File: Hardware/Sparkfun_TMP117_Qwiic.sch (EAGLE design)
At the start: 22 parts, among them J1 PTH, U2 TMP117

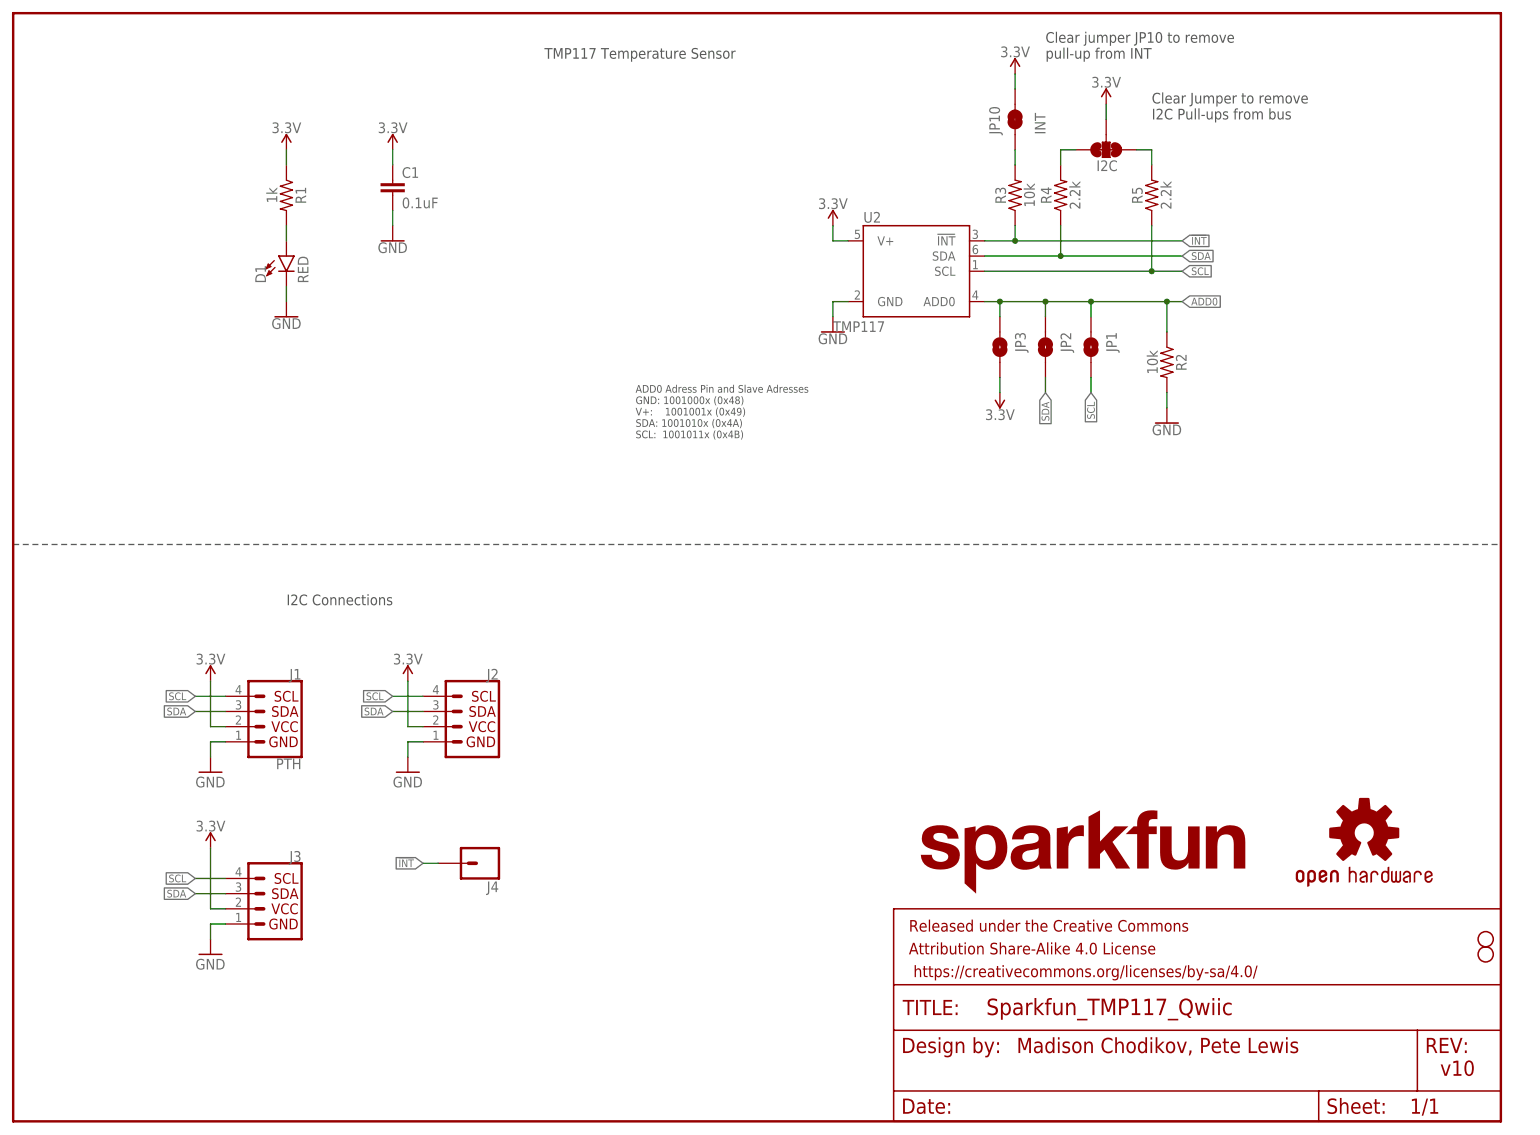
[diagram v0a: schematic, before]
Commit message: more layout changes
-moved to 4 jumpers on address select, to fully remove pull resisor when you cut trace. Previous version had pull down resistor permenantly in circuit, so it would be tied to SDA or SCL when those address options were selected.
-SCH cleanup
-rerouting as necessary.
-added LED bypass jumper
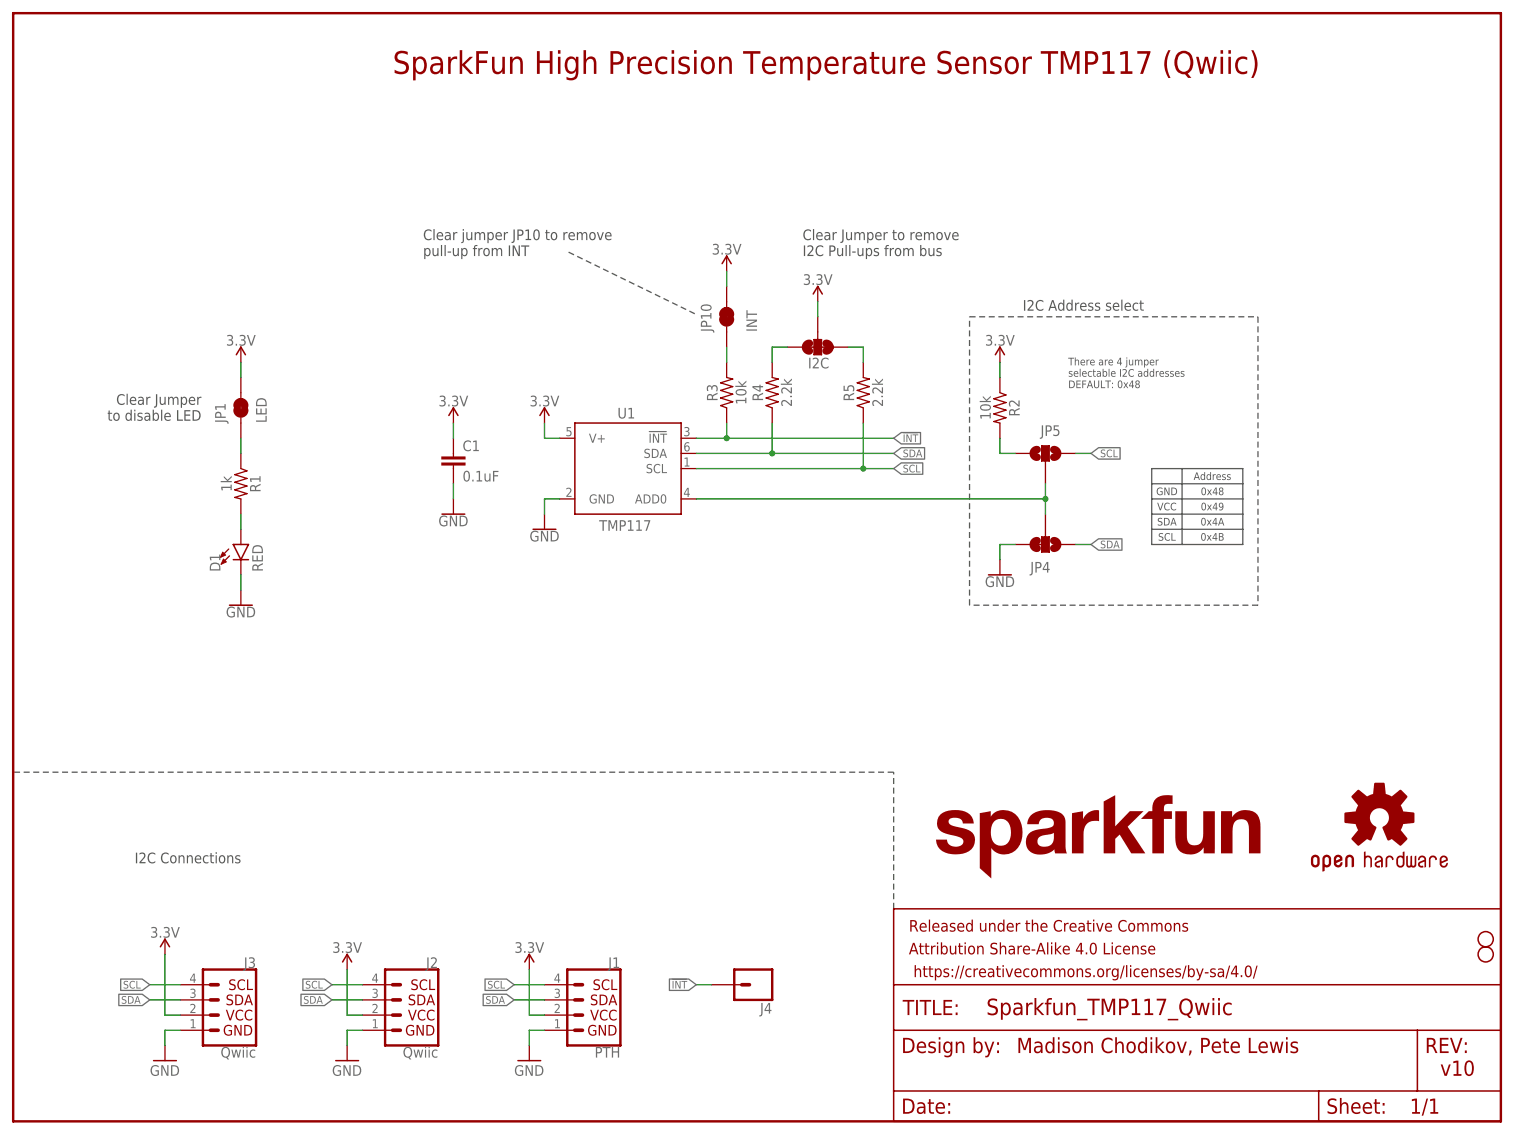
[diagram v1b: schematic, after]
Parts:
- removed JP2, JP3: JUMPER-SMT_2_NO_SILK, SparkFun-Jumpers:JUMPER-SMT_2_NO_SILK
- removed U2: TMP117, TMP117:TMP117
- added JP4: JUMPER-SMT_3_1-NC_TRACE_NO-SILK, SparkFun-Jumpers:JUMPER-SMT_3_1-NC_TRACE_NO-SILK
- added JP5: JUMPER-SMT_3_NO_NO_SILK, SparkFun-Jumpers:JUMPER-SMT_3_NO_NO_SILK
- added U1: TMP117, TMP117:TMP117
- J2, J3: value (none) -> Qwiic
- JP1: value JUMPER-SMT_2_NO_SILK -> LED; device SparkFun-Jumpers:JUMPER-SMT_2_NO_SILK -> SparkFun-Jumpers:JUMPER-SMT_2_NC_TRACE_SILK
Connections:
- new net N$7: JP5.1, R2.2
- new net N$8: JP1.1, R1.1
- net !INT: now also U1.!INT; no longer U2.!INT
- net 3.3V: now also JP1.2, R2.1, U1.V+; no longer JP3.2, R1.1, U2.V+
- net ADD0: now also JP4.2, JP5.2, U1.ADD0; no longer JP1.1, JP2.1, JP3.1, R2.1, U2.ADD0
- net GND: now also JP4.3, U1.GND; no longer R2.2, U2.GND
- net SCL: now also JP5.3, U1.SCL; no longer JP1.2, U2.SCL
- net SDA: now also JP4.1, U1.SDA; no longer JP2.2, U2.SDA
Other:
- note added: "0x48"
- note added: "0x49"
- note added: "0x4A"
- note added: "0x4B"
- note added: "Address"
- note added: "Clear Jumper to disable LED"
- note added: "GND"
- note added: "I2C Address select"
- note added: "SCL"
- note added: "SDA"
- note added: "SparkFun High Precision Temperature Sensor TMP117 (Qwiic)"
- note added: "There are 4 jumper selectable I2C addresses DEFAULT: 0x48"
- note added: "VCC"
- note removed: "ADD0 Adress Pin and Slave Adresses GND: 1001000x (0x48) V+: 1001001x (0x49) SDA: 1001010x (0x4A) SCL: 1001011x (0x4B)"
- note removed: "TMP117 Temperature Sensor"
- moved on the sheet: C1, D1, I2C, J1, J2, J3, J4, JP10, R1, R2, R3, R4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

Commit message: post design review changes
-Added fiducials
-added bottom two standoffs
-switched to SFE logo with flame
-moved I2C jumper to bottom
-added outer box silk to address jumpers
-moved pwr LED and jumper to make room for standoff
-changes all traces to 8 mil, except 3.3V power up to 16 mil.
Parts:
- removed LOGO2: SFE_LOGO_NAME.1_INCH, SparkFun-Aesthetics:SFE_LOGO_NAME.1_INCH
- added FD1, FD2, FD3, FD4: FIDUCIALUFIDUCIAL, SparkFun-Aesthetics:FIDUCIALUFIDUCIAL
- added JP2, JP3: STAND-OFF, SparkFun:STAND-OFF
- added LOGO4: SFE_LOGO_NAME_FLAME.1_INCH, SparkFun-Aesthetics:SFE_LOGO_NAME_FLAME.1_INCH
- JP10: device SparkFun-Passives:JUMPER-PAD-2-NC_BY_TRACE -> SparkFun-Jumpers:JUMPER-SMT_2_NC_TRACE_SILK
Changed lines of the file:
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@@
 <part name="JP9" library="SparkFun" deviceset="STAND-OFF" device=""/>
 <part name="I2C" library="SparkFun-Jumpers" library_urn="urn:adsk.eagle:library:528" deviceset="JUMPER-SMT_3_2-NC_TRACE" device="_SILK" package3d_urn="urn:adsk.eagle:package:39289/1" value=""/>
-<part name="JP10" library="SparkFun-Passives" deviceset="JUMPER-PAD-2-NC_BY_TRACE" device="" value="INT"/>
+<part name="JP10" library="SparkFun-Jumpers" deviceset="JUMPER-SMT_2_NC_TRACE" device="_SILK" value="INT"/>
 <part name="U1" library="TMP117" deviceset="TMP117" device=""/>
-<part name="LOGO2" library="SparkFun-Aesthetics" deviceset="SFE_LOGO_NAME" device=".1_INCH"/>
 <part name="JP4" library="SparkFun-Jumpers" deviceset="JUMPER-SMT_3_1-NC_TRACE" device="_NO-SILK"/>
 <part name="GND8" library="SparkFun-PowerSymbols" deviceset="GND" device=""/>
@@
 <part name="SUPPLY10" library="SparkFun-PowerSymbols" library_urn="urn:adsk.eagle:library:530" deviceset="3.3V" device=""/>
 <part name="JP1" library="SparkFun-Jumpers" library_urn="urn:adsk.eagle:library:528" deviceset="JUMPER-SMT_2_NC_TRACE" device="_SILK" package3d_urn="urn:adsk.eagle:package:39281/1" value="LED"/>
+<part name="JP2" library="SparkFun" deviceset="STAND-OFF" device=""/>
+<part name="JP3" library="SparkFun" deviceset="STAND-OFF" device=""/>
+<part name="LOGO4" library="SparkFun-Aesthetics" deviceset="SFE_LOGO_NAME_FLAME" device=".1_INCH"/>
+<part name="FD1" library="SparkFun-Aesthetics" library_urn="urn:adsk.eagle:library:507" deviceset="FIDUCIAL" device="UFIDUCIAL" package3d_urn="urn:adsk.eagle:package:37111/1"/>
+<part name="FD2" library="SparkFun-Aesthetics" library_urn="urn:adsk.eagle:library:507" deviceset="FIDUCIAL" device="UFIDUCIAL" package3d_urn="urn:adsk.eagle:package:37111/1"/>
+<part name="FD3" library="SparkFun-Aesthetics" library_urn="urn:adsk.eagle:library:507" deviceset="FIDUCIAL" device="UFIDUCIAL" package3d_urn="urn:adsk.eagle:package:37111/1"/>
+<part name="FD4" library="SparkFun-Aesthetics" library_urn="urn:adsk.eagle:library:507" deviceset="FIDUCIAL" device="UFIDUCIAL" package3d_urn="urn:adsk.eagle:package:37111/1"/>
 </parts>
 <sheets>
@@
 <attribute name="VALUE" x="98.044" y="98.806" size="1.778" layer="96"/>
 </instance>
-<instance part="LOGO2" gate="G$1" x="152.4" y="40.64" smashed="yes"/>
 <instance part="JP4" gate="G$1" x="172.72" y="96.52" smashed="yes" rot="R270">
 <attribute name="NAME" x="170.18" y="91.821" size="1.778" layer="95" font="vector"/>
@@
 <attribute name="VALUE" x="40.64" y="116.84" size="1.778" layer="96" font="vector" rot="R90" align="top-left"/>
 </instance>
+<instance part="JP2" gate="G$1" x="243.84" y="30.48" smashed="yes"/>
+<instance part="JP3" gate="G$1" x="243.84" y="27.94" smashed="yes"/>
+<instance part="LOGO4" gate="G$1" x="152.4" y="38.1" smashed="yes"/>
+<instance part="FD1" gate="G$1" x="238.76" y="30.48" smashed="yes"/>
+<instance part="FD2" gate="G$1" x="241.3" y="30.48" smashed="yes"/>
+<instance part="FD3" gate="G$1" x="238.76" y="27.94" smashed="yes"/>
+<instance part="FD4" gate="G$1" x="241.3" y="27.94" smashed="yes"/>
 </instances>
 <busses>

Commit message: parts to SFE libraries
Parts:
- J1: device SparkX:I2C_STANDARD_NO_SILK -> SparkFun-Connectors:I2C_STANDARD_NO_SILK
- J2, J3: value Qwiic -> QWIIC_RA
- U1: device TMP117:TMP117 -> SparkFun-Sensors:TMP117
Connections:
- net 3.3V: now also J1.2; no longer J1.VCC
- net GND: now also J1.1; no longer J1.GND
- net SCL: now also J1.4; no longer J1.SCL
- net SDA: now also J1.3; no longer J1.SDA
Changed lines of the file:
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@@
 <part name="C1" library="SparkFun-Capacitors" deviceset="0.1UF" device="-0603-25V-(+80/-20%)" value="0.1uF"/>
 <part name="GND4" library="SparkFun-PowerSymbols" deviceset="GND" device=""/>
-<part name="J1" library="SparkX" deviceset="I2C_STANDARD" device="_NO_SILK" value="PTH"/>
-<part name="J3" library="SparkFun-Connectors" deviceset="QWIIC_CONNECTOR" device="JS-1MM" value="Qwiic"/>
+<part name="J1" library="SparkFun-Connectors" deviceset="I2C_STANDARD" device="_NO_SILK" value="PTH"/>
+<part name="J3" library="SparkFun-Connectors" deviceset="QWIIC_CONNECTOR" device="JS-1MM" value="QWIIC_RA"/>
 <part name="J4" library="SparkFun-Connectors" deviceset="CONN_01" device="PTH_NO_SILK_YES_STOP"/>
 <part name="LOGO1" library="SparkFun-Aesthetics" deviceset="OSHW-LOGO" device="MINI"/>
@@
 <part name="SUPPLY8" library="SparkFun-PowerSymbols" library_urn="urn:adsk.eagle:library:530" deviceset="3.3V" device=""/>
 <part name="SUPPLY9" library="SparkFun-PowerSymbols" library_urn="urn:adsk.eagle:library:530" deviceset="3.3V" device=""/>
-<part name="J2" library="SparkFun-Connectors" deviceset="QWIIC_CONNECTOR" device="JS-1MM" value="Qwiic"/>
+<part name="J2" library="SparkFun-Connectors" deviceset="QWIIC_CONNECTOR" device="JS-1MM" value="QWIIC_RA"/>
 <part name="JP8" library="SparkFun" deviceset="STAND-OFF" device=""/>
 <part name="JP9" library="SparkFun" deviceset="STAND-OFF" device=""/>
 <part name="I2C" library="SparkFun-Jumpers" library_urn="urn:adsk.eagle:library:528" deviceset="JUMPER-SMT_3_2-NC_TRACE" device="_SILK" package3d_urn="urn:adsk.eagle:package:39289/1" value=""/>
 <part name="JP10" library="SparkFun-Jumpers" deviceset="JUMPER-SMT_2_NC_TRACE" device="_SILK" value="INT"/>
-<part name="U1" library="TMP117" deviceset="TMP117" device=""/>
+<part name="U1" library="SparkFun-Sensors" deviceset="TMP117" device=""/>
 <part name="JP4" library="SparkFun-Jumpers" deviceset="JUMPER-SMT_3_1-NC_TRACE" device="_NO-SILK"/>
 <part name="GND8" library="SparkFun-PowerSymbols" deviceset="GND" device=""/>
@@
 <pinref part="GND5" gate="1" pin="GND"/>
 <wire x1="86.36" y1="12.7" x2="86.36" y2="15.24" width="0.1524" layer="91"/>
-<pinref part="J1" gate="G$1" pin="GND"/>
+<pinref part="J1" gate="G$1" pin="1"/>
 <wire x1="86.36" y1="15.24" x2="88.9" y2="15.24" width="0.1524" layer="91"/>
 </segment>
@@
 <pinref part="SUPPLY3" gate="G$1" pin="3.3V"/>
 <wire x1="86.36" y1="25.4" x2="86.36" y2="17.78" width="0.1524" layer="91"/>
-<pinref part="J1" gate="G$1" pin="VCC"/>
+<pinref part="J1" gate="G$1" pin="2"/>
 <wire x1="86.36" y1="17.78" x2="88.9" y2="17.78" width="0.1524" layer="91"/>
 </segment>
@@
 <net name="SDA" class="0">
 <segment>
-<pinref part="J1" gate="G$1" pin="SDA"/>
+<pinref part="J1" gate="G$1" pin="3"/>
 <wire x1="83.82" y1="20.32" x2="88.9" y2="20.32" width="0.1524" layer="91"/>
 <label x="83.82" y="20.32" size="1.27" layer="95" rot="R180" xref="yes"/>
@@
 </segment>
 <segment>
-<pinref part="J1" gate="G$1" pin="SCL"/>
+<pinref part="J1" gate="G$1" pin="4"/>
 <wire x1="88.9" y1="22.86" x2="83.82" y2="22.86" width="0.1524" layer="91"/>
 <label x="83.82" y="22.86" size="1.27" layer="95" rot="R180" xref="yes"/>

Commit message: 1st run of checklist
-version font type in schematic
-silk width bumped up to 8 mils on a couple jumpers and the tmp117 package
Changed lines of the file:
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@@
 <part name="JP8" library="SparkFun" deviceset="STAND-OFF" device=""/>
 <part name="JP9" library="SparkFun" deviceset="STAND-OFF" device=""/>
-<part name="I2C" library="SparkFun-Jumpers" library_urn="urn:adsk.eagle:library:528" deviceset="JUMPER-SMT_3_2-NC_TRACE" device="_SILK" package3d_urn="urn:adsk.eagle:package:39289/1" value=""/>
-<part name="JP10" library="SparkFun-Jumpers" deviceset="JUMPER-SMT_2_NC_TRACE" device="_SILK" value="INT"/>
+<part name="I2C" library="SparkFun-Jumpers" deviceset="JUMPER-SMT_3_2-NC_TRACE" device="_SILK" package3d_urn="urn:adsk.eagle:package:39289/1" value="JUMPER-SMT_3_2-NC_TRACE_SILK"/>
+<part name="JP10" library="SparkFun-Jumpers" deviceset="JUMPER-SMT_2_NC_TRACE" device="_SILK" package3d_urn="urn:adsk.eagle:package:39281/1" value="INT"/>
 <part name="U1" library="SparkFun-Sensors" deviceset="TMP117" device=""/>
 <part name="JP4" library="SparkFun-Jumpers" deviceset="JUMPER-SMT_3_1-NC_TRACE" device="_NO-SILK"/>
@@
 <part name="JP5" library="SparkFun-Jumpers" deviceset="JUMPER-SMT_3_NO" device="_NO_SILK" value="JUMPER-SMT_3_NO_NO_SILK"/>
 <part name="SUPPLY10" library="SparkFun-PowerSymbols" library_urn="urn:adsk.eagle:library:530" deviceset="3.3V" device=""/>
-<part name="JP1" library="SparkFun-Jumpers" library_urn="urn:adsk.eagle:library:528" deviceset="JUMPER-SMT_2_NC_TRACE" device="_SILK" package3d_urn="urn:adsk.eagle:package:39281/1" value="LED"/>
+<part name="JP1" library="SparkFun-Jumpers" deviceset="JUMPER-SMT_2_NC_TRACE" device="_SILK" package3d_urn="urn:adsk.eagle:package:39281/1" value="LED"/>
 <part name="JP2" library="SparkFun" deviceset="STAND-OFF" device=""/>
 <part name="JP3" library="SparkFun" deviceset="STAND-OFF" device=""/>
@@
 <text x="68.58" y="144.78" size="1.778" layer="97" font="vector">Clear jumper JP10 to remove
 pull-up from INT</text>
-<text x="238.76" y="7.62" size="2.54" layer="94">v10</text>
+<text x="238.76" y="7.62" size="2.54" layer="94" font="vector">v10</text>
 <text x="176.53" y="122.682" size="1.27" layer="97" font="vector">There are 4 jumper
 selectable I2C addresses

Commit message: checklist catches
-remove package value on jumpers (SCH)
-added VCC range text obj
-fixed drc errors cause by unconnected dimension wires on special route out stuff near IC
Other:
- note added: "(When using other qwiic ecosystem boards, only use 3.3V)"
- note added: "Madison Chodikov"
- note added: "Revised by: Pete Lewis"
- note added: "VCC RANGE: 1.8V to 5.5V"
- note removed: "Madison Chodikov, Pete Lewis"
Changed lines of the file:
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@@
 <part name="JP8" library="SparkFun" deviceset="STAND-OFF" device=""/>
 <part name="JP9" library="SparkFun" deviceset="STAND-OFF" device=""/>
-<part name="I2C" library="SparkFun-Jumpers" deviceset="JUMPER-SMT_3_2-NC_TRACE" device="_SILK" package3d_urn="urn:adsk.eagle:package:39289/1" value="JUMPER-SMT_3_2-NC_TRACE_SILK"/>
+<part name="I2C" library="SparkFun-Jumpers" deviceset="JUMPER-SMT_3_2-NC_TRACE" device="_SILK" package3d_urn="urn:adsk.eagle:package:39289/1" value=""/>
 <part name="JP10" library="SparkFun-Jumpers" deviceset="JUMPER-SMT_2_NC_TRACE" device="_SILK" package3d_urn="urn:adsk.eagle:package:39281/1" value="INT"/>
 <part name="U1" library="SparkFun-Sensors" deviceset="TMP117" device=""/>
@@
 <text x="20.32" y="43.18" size="1.778" layer="97" font="vector">I2C Connections</text>
 <text x="63.5" y="175.26" size="3.81" layer="94" font="vector">SparkFun High Precision Temperature Sensor TMP117 (Qwiic)</text>
-<text x="167.894" y="11.43" size="2.54" layer="94" font="vector">Madison Chodikov, Pete Lewis</text>
+<text x="167.894" y="11.43" size="2.54" layer="94" font="vector">Madison Chodikov</text>
 <text x="132.08" y="144.78" size="1.778" layer="97" font="vector">Clear Jumper to remove
 I2C Pull-ups from bus</text>
@@
 <wire x1="195.58" y1="109.22" x2="195.58" y2="96.52" width="0.2032" layer="97"/>
 <text x="200.66" y="107.95" size="1.27" layer="97" font="vector" align="center">Address</text>
-<text x="200.66" y="105.41" size="1.27" layer="97" font="vector" align="center">0x48</text>
+<text x="200.66" y="105.41" size="1.27" layer="97" font="vector" ratio="15" align="center">0x48</text>
 <text x="200.66" y="102.87" size="1.27" layer="97" font="vector" align="center">0x49</text>
 <text x="200.66" y="100.33" size="1.27" layer="97" font="vector" align="center">0x4A</text>
 <text x="200.66" y="97.79" size="1.27" layer="97" font="vector" align="center">0x4B</text>
-<text x="193.04" y="105.41" size="1.27" layer="97" font="vector" align="center">GND</text>
+<text x="193.04" y="105.41" size="1.27" layer="97" font="vector" ratio="15" align="center">GND</text>
 <text x="193.04" y="102.87" size="1.27" layer="97" font="vector" align="center">VCC</text>
 <text x="193.04" y="100.33" size="1.27" layer="97" font="vector" align="center">SDA</text>
@@
 <wire x1="147.32" y1="35.56" x2="147.32" y2="58.42" width="0.1524" layer="97" style="shortdash"/>
 <wire x1="147.32" y1="58.42" x2="0" y2="58.42" width="0.1524" layer="97" style="shortdash"/>
+<text x="167.64" y="7.62" size="2.54" layer="94" font="vector">Revised by: Pete Lewis</text>
+<text x="83.82" y="88.9" size="2.54" layer="97" font="vector">VCC RANGE: 1.8V to 5.5V</text>
+<text x="81.28" y="81.28" size="1.778" layer="97" font="vector">(When using other qwiic
+ecosystem boards, only use 3.3V)</text>
 </plain>
 <instances>
